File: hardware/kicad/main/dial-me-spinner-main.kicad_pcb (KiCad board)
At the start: 4 copper layers, 64 x 64 mm, 204 parts, among them J1 LINK, J10 SWD, J20 OLED_ZIF30, J40 MOTOR, U1 RT9080-33GJ5, U10 MDBT50Q-U1MV2, U11 W25Q128JVSIQ, U2 TPS22917DBVR, U20 TPS61040DBVR, U21 TPS22917DBVR, U30 TMAG5273A2QDBVR, U31 LIS2DW12TR, U32 TPD4E05U06DQAR, U40 DRV8837DSGR, U41 DRV8837DSGR, U42 DRV5032FADBZR, U43 SN74LV1T34DBVR, Y1 32.768k 9pF

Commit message: NFC tag: P0.09/P0.10 as NFC1/NFC2 with 180 pF tuning caps and coil pads; CHG_INT_N moves to P1.03
Co-Authored-By: Claude Opus 5.5 <noreply@anthropic.com>
Claude-Session: https://claude.ai/code/session_01P3cqdBhxLcWY3sGUVf9LAJ
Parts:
- added C16: 180p C0G, Capacitor_SMD:C_0402_1005Metric, B.Cu at (87.3, 120.2)
- added C17: 180p C0G, Capacitor_SMD:C_0402_1005Metric, B.Cu at (84.9, 120.2)
- added J11: NFC_COIL, dial_spinner:NFC_Coil_Pads_1x02_P2.0mm, F.Cu at (84.0, 114.4)
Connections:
- U10 pad 52: CHG_INT_N -> /MCU, flash & debug/NFC1
- U10 pad 54: unconnected-(U10-P0.10-Pad54) -> /MCU, flash & debug/NFC2
- U10 pad 60: unconnected-(U10-P1.03-Pad60) -> CHG_INT_N

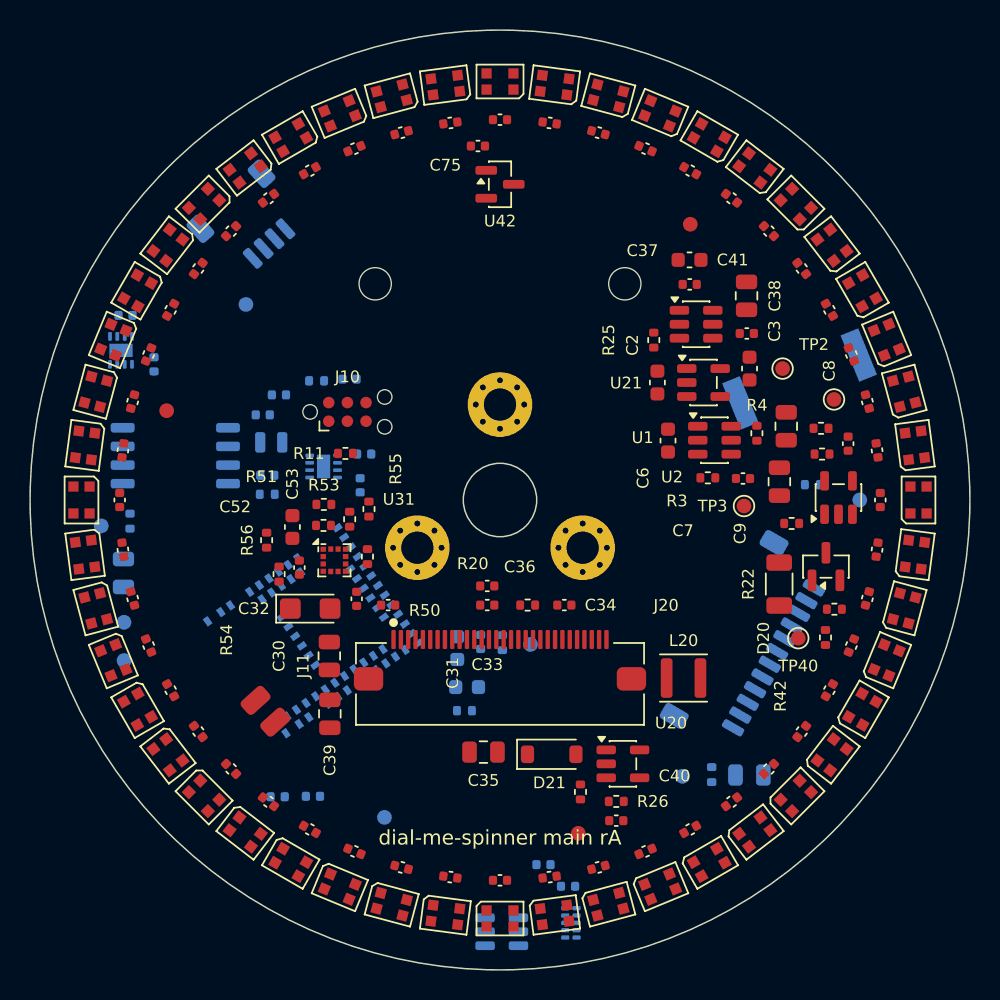
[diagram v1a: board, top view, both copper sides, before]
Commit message: Main board: pin anchors may use the opposite side over the pad (R40 now 0.6 mm from P0.06 on top); U12 anchored at the module D-
Co-Authored-By: Claude Opus 5.5 <noreply@anthropic.com>
Claude-Session: https://claude.ai/code/session_01P3cqdBhxLcWY3sGUVf9LAJ
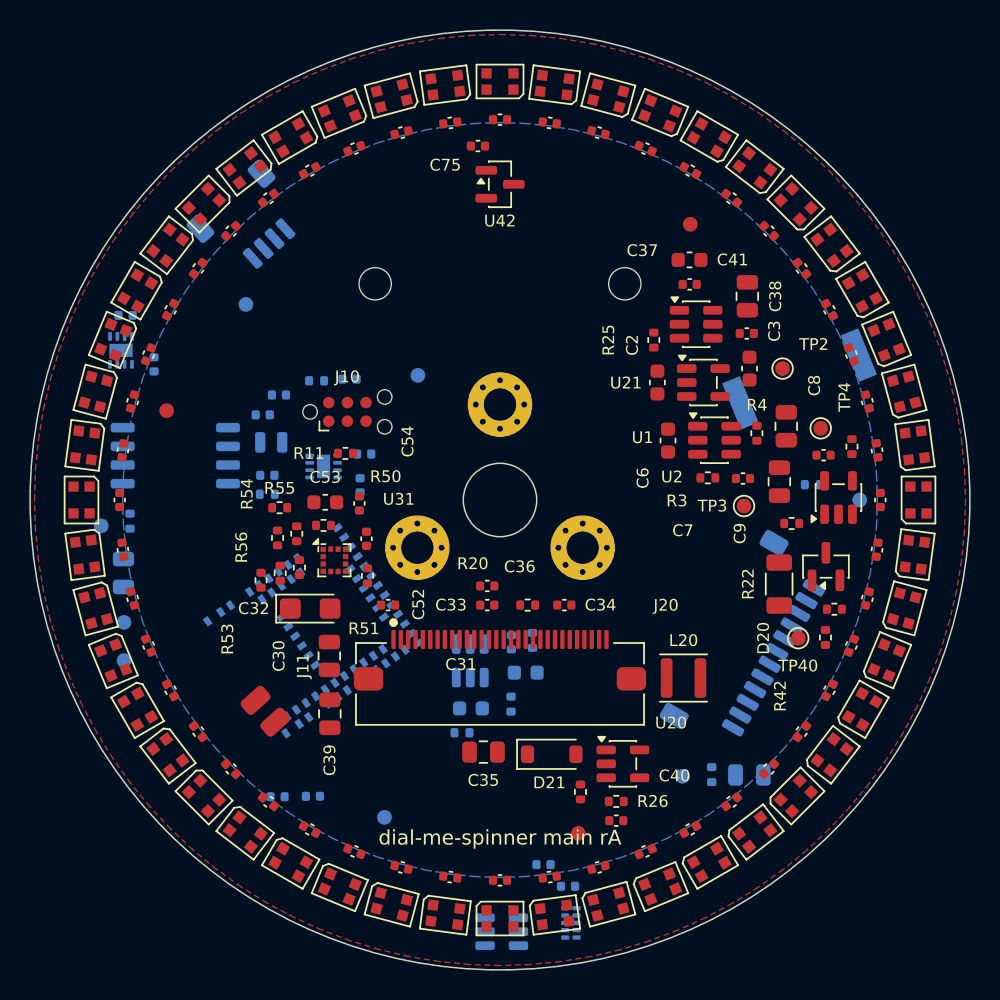
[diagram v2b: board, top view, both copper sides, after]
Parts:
- added R12: 4.7, Resistor_SMD:R_0402_1005Metric, B.Cu at (102.2, 109.6)
- added U12: USBLC6-2SC6, Package_TO_SOT_SMD:SOT-23-6, B.Cu at (98.0, 111.0)
- C2, C41, C6: value 10u -> 10u/25V
- R4: value 100 -> 68
- moved R40 29.1 mm to (91.0, 105.2), turned to 90 degrees
- moved TP11 19.9 mm to (94.4, 91.5)
- moved R57 6.72 mm to (97.4, 115.8), turned to 0 degrees
- moved C54 6.50 mm to (90.4, 100.2)
- moved R55 6.08 mm to (85.0, 100.5), turned to 0 degrees
- moved R53 5.55 mm to (85.0, 105.0), turned to 90 degrees
- moved R41 5.16 mm to (119.9, 101.6)
- moved C52 4.97 mm to (90.9, 102.6)
- moved C10 4.21 mm to (98.0, 114.2), turned to 0 degrees
- moved C12 4.11 mm to (101.8, 111.8)
- moved R52 3.74 mm to (86.2, 102.3)
- moved R50 3.67 mm to (88.0, 101.7), turned to 0 degrees
- moved R51 3.31 mm to (86.3, 104.6), turned to 90 degrees
- moved R58 3.20 mm to (100.8, 113.9), turned to 90 degrees
- moved C53 2.80 mm to (88.1, 100.2), turned to 0 degrees
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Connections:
- C12 pad 1: VBUS -> /MCU, flash & debug/VBUS_NRF
- U10 pad 32: VBUS -> /MCU, flash & debug/VBUS_NRF
- U21 pad 5: unconnected-(U21-QOD-Pad5) -> OLED_VIN
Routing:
- added copper zone on B.Cu, net GND
- added copper zone on F.Cu, net GND

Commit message: WIP: main board routing in progress
Co-Authored-By: Claude Opus 5.5 <noreply@anthropic.com>
Claude-Session: https://claude.ai/code/session_01P3cqdBhxLcWY3sGUVf9LAJ
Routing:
- removed copper zone on B.Cu, net GND
- removed copper zone on F.Cu, net GND

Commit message: WIP: main board routing (attempt 2 in progress)
Co-Authored-By: Claude Opus 5.5 <noreply@anthropic.com>
Claude-Session: https://claude.ai/code/session_01P3cqdBhxLcWY3sGUVf9LAJ
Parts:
- turned C106 to 128 degrees
- turned C132 to -37 degrees
- turned C142 to 38 degrees
- turned C144 to 53 degrees
- turned C118 to -142 degrees
- turned C120 to -127 degrees
- turned C108 to 143 degrees
- turned C130 to -52 degrees
- turned D140 to 23 degrees
- turned D146 to 68 degrees
- turned D104 to 113 degrees
- turned D134 to -22 degrees
- turned D110 to 158 degrees
- turned D128 to -67 degrees
- turned D116 to -157 degrees
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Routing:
- net GND: track 0.00 -> 758.8 mm, vias 0 -> 8
- net VLED: track 0.00 -> 332.9 mm, vias 0 -> 2
- net +3V3: track 0.00 -> 225.7 mm, vias 0 -> 11
- net VSYS: track 0.00 -> 146.5 mm, vias 0 -> 4
- net I2C_SDA: track 0.00 -> 64.3 mm, vias 0 -> 4
- net HOME_N: track 0.00 -> 47.2 mm, vias 0 -> 3
- net TMAG_INT_N: track 0.00 -> 47.1 mm, vias 0 -> 3
- net LED_PWR_EN: track 0.00 -> 41.7 mm, vias 0 -> 3
- net /LED ring/LED_DIN_R: track 0.00 -> 40.3 mm, vias 0 -> 2
- net I2C_SCL: track 0.00 -> 39.9 mm, vias 0 -> 1
- net OLED_VIN: track 0.00 -> 39.1 mm, vias 0 -> 2
- net +13V_OLED: track 0.00 -> 37.6 mm
- net MOT_B_IN1: track 0.00 -> 31.1 mm, vias 0 -> 2
- net TMAG_SDA: track 0.00 -> 29.0 mm, vias 0 -> 3
- net TMAG_SCL: track 0.00 -> 27.2 mm
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
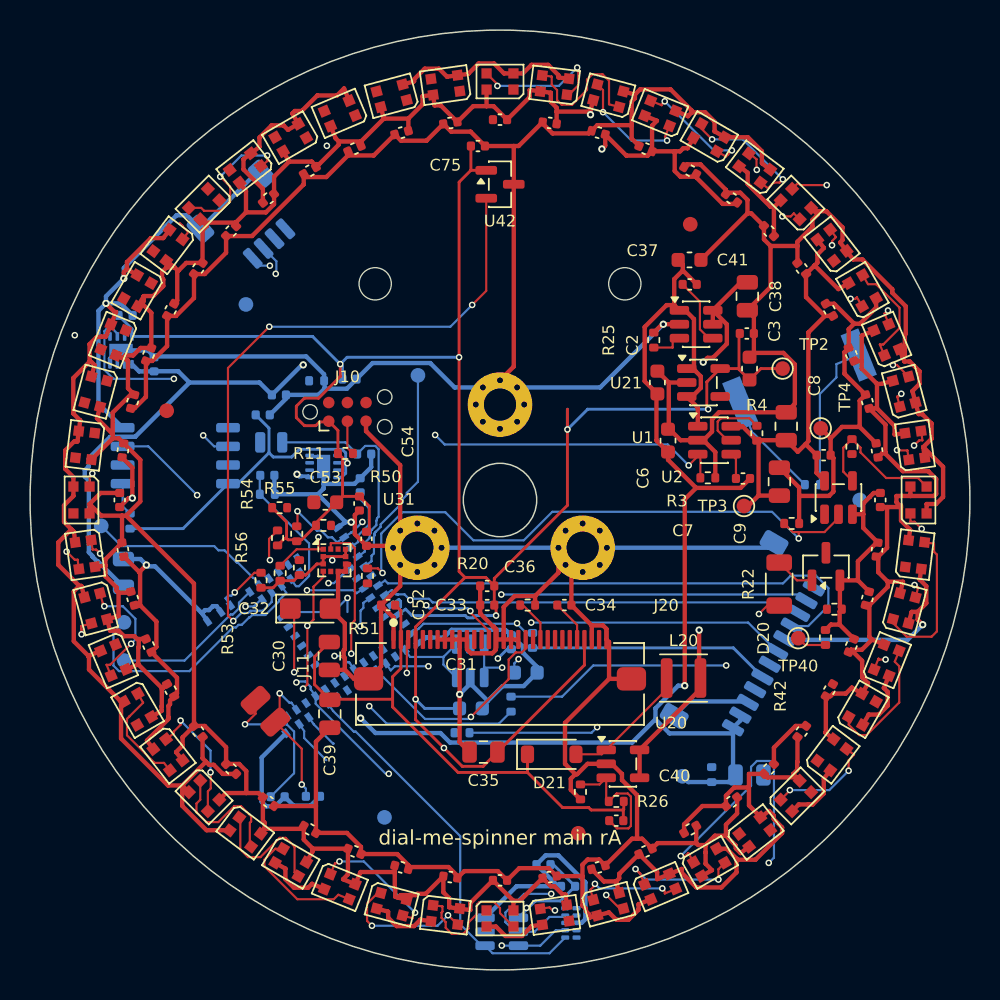
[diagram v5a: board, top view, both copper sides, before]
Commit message: WIP: main board re-placed with GND fan-out (routing), firmware-guard tests in progress
Co-Authored-By: Claude Opus 5.5 <noreply@anthropic.com>
Claude-Session: https://claude.ai/code/session_01P3cqdBhxLcWY3sGUVf9LAJ
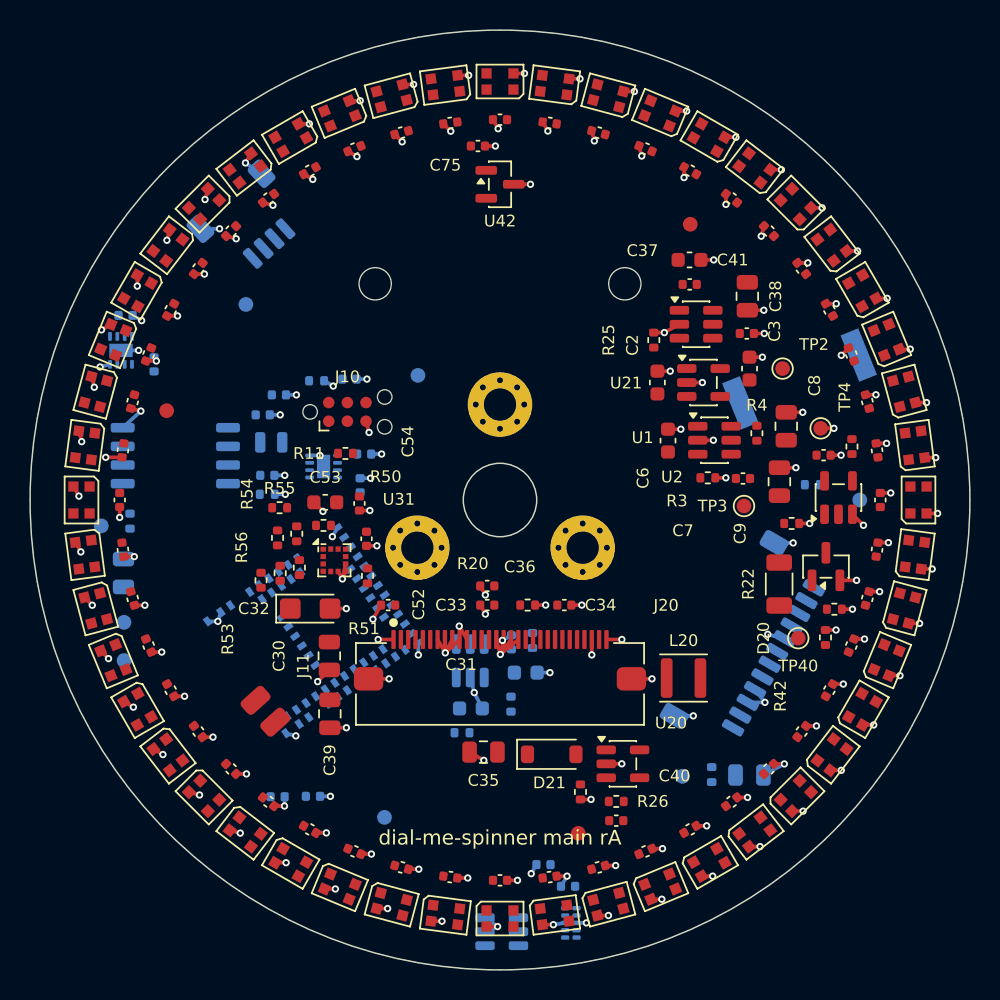
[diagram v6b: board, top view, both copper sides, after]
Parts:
- turned C106 to 127.5 degrees
- turned C132 to -37.5 degrees
- turned C142 to 37.5 degrees
- turned C144 to 52.5 degrees
- turned C118 to -142.5 degrees
- turned C120 to -127.5 degrees
- turned C108 to 142.5 degrees
- turned C130 to -52.5 degrees
- turned D140 to 22.5 degrees
- turned D146 to 67.5 degrees
- turned D104 to 112.5 degrees
- turned D134 to -22.5 degrees
- turned D110 to 157.5 degrees
- turned D128 to -67.5 degrees
- turned D116 to -157.5 degrees
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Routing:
- net GND: track 758.8 -> 157.8 mm, vias 8 -> 168
- net VLED: track 332.9 -> 0.00 mm, vias 2 -> 0
- net +3V3: track 225.7 -> 0.00 mm, vias 11 -> 0
- net VSYS: track 146.5 -> 0.00 mm, vias 4 -> 0
- net I2C_SDA: track 64.3 -> 0.00 mm, vias 4 -> 0
- net HOME_N: track 47.2 -> 0.00 mm, vias 3 -> 0
- net TMAG_INT_N: track 47.1 -> 0.00 mm, vias 3 -> 0
- net LED_PWR_EN: track 41.7 -> 0.00 mm, vias 3 -> 0
- net /LED ring/LED_DIN_R: track 40.3 -> 0.00 mm, vias 2 -> 0
- net I2C_SCL: track 39.9 -> 0.00 mm, vias 1 -> 0
- net OLED_VIN: track 39.1 -> 0.00 mm, vias 2 -> 0
- net +13V_OLED: track 37.6 -> 0.00 mm
- net MOT_B_IN1: track 31.1 -> 0.00 mm, vias 2 -> 0
- net TMAG_SDA: track 29.0 -> 0.00 mm, vias 3 -> 0
- net TMAG_SCL: track 27.2 -> 0.00 mm
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
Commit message: WIP: main board routing (attempt 2), firmware-guard SPICE tests and xdist results merge in progress
Co-Authored-By: Claude Opus 5.5 <noreply@anthropic.com>
Claude-Session: https://claude.ai/code/session_01P3cqdBhxLcWY3sGUVf9LAJ
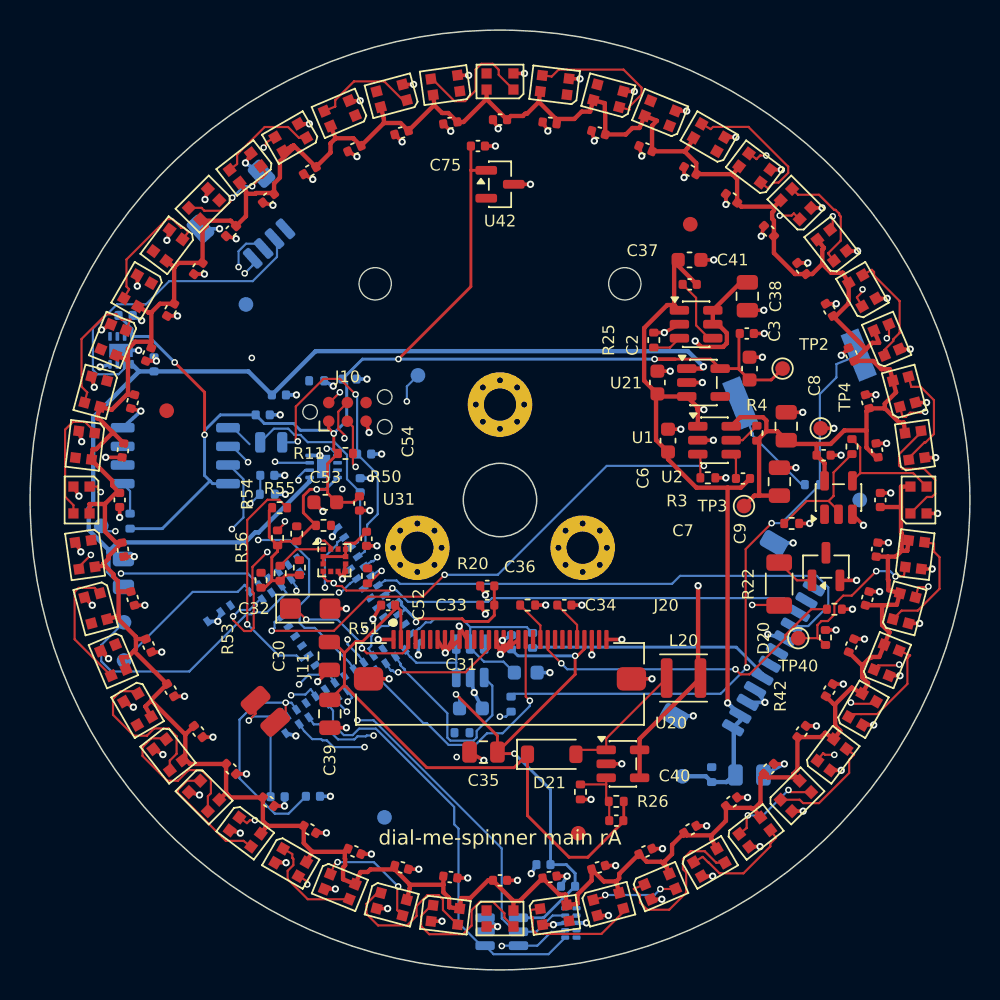
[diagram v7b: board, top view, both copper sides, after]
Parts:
- turned C106 to 128 degrees
- turned C132 to -37 degrees
- turned C142 to 38 degrees
- turned C144 to 53 degrees
- turned C118 to -142 degrees
- turned C120 to -127 degrees
- turned C108 to 143 degrees
- turned C130 to -52 degrees
- turned D140 to 23 degrees
- turned D146 to 68 degrees
- turned D104 to 113 degrees
- turned D134 to -22 degrees
- turned D110 to 158 degrees
- turned D128 to -67 degrees
- turned D116 to -157 degrees
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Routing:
- net VLED: track 0.00 -> 294.6 mm
- net +3V3: track 0.00 -> 176.6 mm, vias 0 -> 10
- net VSYS: track 0.00 -> 133.0 mm, vias 0 -> 3
- net I2C_SDA: track 0.00 -> 42.2 mm, vias 0 -> 3
- net /Sensors & sounder/BZ_N: track 0.00 -> 42.2 mm, vias 0 -> 2
- net +13V_OLED: track 0.00 -> 41.9 mm
- net OLED_VIN: track 0.00 -> 40.4 mm, vias 0 -> 2
- net I2C_SCL: track 0.00 -> 39.1 mm
- net TMAG_INT_N: track 0.00 -> 37.3 mm, vias 0 -> 2
- net LED_PWR_EN: track 0.00 -> 37.3 mm, vias 0 -> 3
- net /MCU, flash & debug/SWDIO: track 0.00 -> 31.0 mm, vias 0 -> 2
- net /MCU, flash & debug/SWDCLK: track 0.00 -> 30.1 mm, vias 0 -> 2
- net TMAG_SDA: track 0.00 -> 29.9 mm, vias 0 -> 2
- net TMAG_SCL: track 0.00 -> 29.1 mm
- net /OLED display & 13 V boost/OLED_IREF: track 0.00 -> 22.4 mm, vias 0 -> 2
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
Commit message: WIP: main board re-placed with finer rules (routing)
Co-Authored-By: Claude Opus 5.5 <noreply@anthropic.com>
Claude-Session: https://claude.ai/code/session_01P3cqdBhxLcWY3sGUVf9LAJ
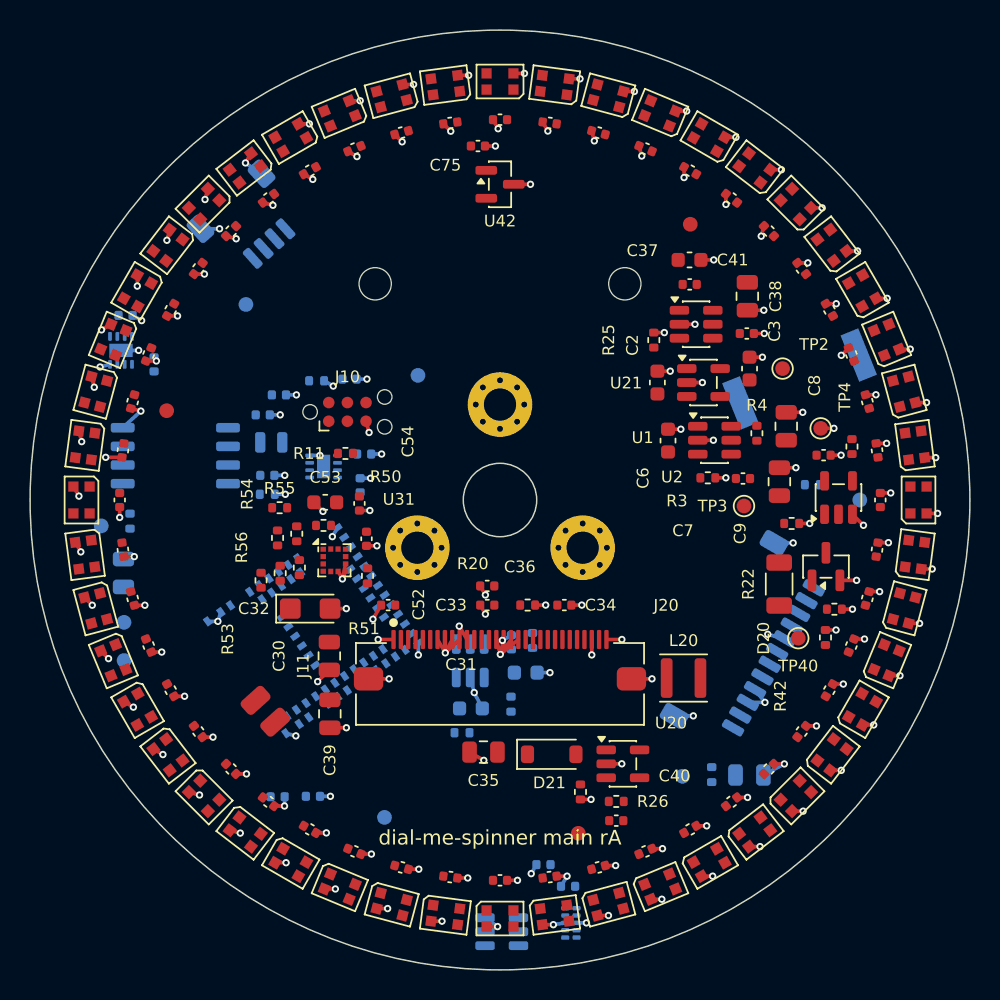
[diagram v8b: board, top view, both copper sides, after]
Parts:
- turned C106 to 127.5 degrees
- turned C132 to -37.5 degrees
- turned C142 to 37.5 degrees
- turned C144 to 52.5 degrees
- turned C118 to -142.5 degrees
- turned C120 to -127.5 degrees
- turned C108 to 142.5 degrees
- turned C130 to -52.5 degrees
- turned D140 to 22.5 degrees
- turned D146 to 67.5 degrees
- turned D104 to 112.5 degrees
- turned D134 to -22.5 degrees
- turned D110 to 157.5 degrees
- turned D128 to -67.5 degrees
- turned D116 to -157.5 degrees
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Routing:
- net VLED: track 294.6 -> 0.00 mm
- net +3V3: track 176.6 -> 0.00 mm, vias 10 -> 0
- net VSYS: track 133.0 -> 0.00 mm, vias 3 -> 0
- net I2C_SDA: track 42.2 -> 0.00 mm, vias 3 -> 0
- net /Sensors & sounder/BZ_N: track 42.2 -> 0.00 mm, vias 2 -> 0
- net +13V_OLED: track 41.9 -> 0.00 mm
- net OLED_VIN: track 40.4 -> 0.00 mm, vias 2 -> 0
- net I2C_SCL: track 39.1 -> 0.00 mm
- net TMAG_INT_N: track 37.3 -> 0.00 mm, vias 2 -> 0
- net LED_PWR_EN: track 37.3 -> 0.00 mm, vias 3 -> 0
- net /MCU, flash & debug/SWDIO: track 31.0 -> 0.00 mm, vias 2 -> 0
- net /MCU, flash & debug/SWDCLK: track 30.1 -> 0.00 mm, vias 2 -> 0
- net TMAG_SDA: track 29.9 -> 0.00 mm, vias 2 -> 0
- net TMAG_SCL: track 29.1 -> 0.00 mm
- net /OLED display & 13 V boost/OLED_IREF: track 22.4 -> 0.00 mm, vias 2 -> 0
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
